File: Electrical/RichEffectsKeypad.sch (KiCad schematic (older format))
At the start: 1 part

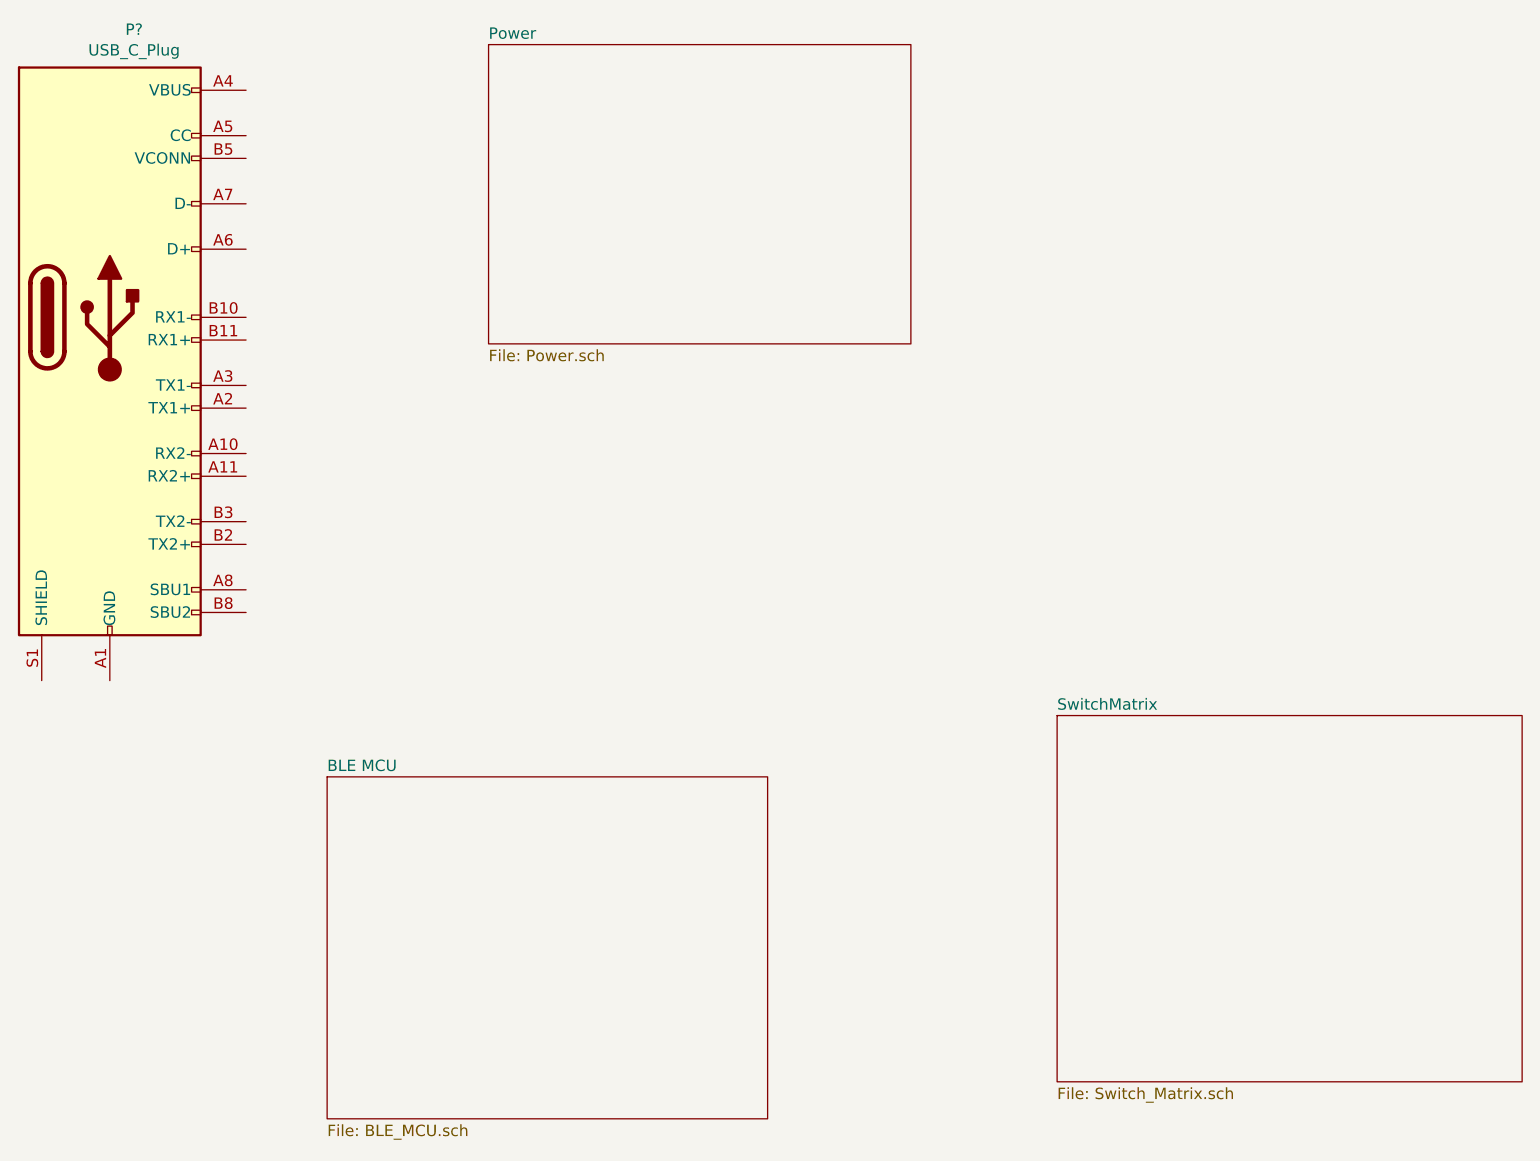
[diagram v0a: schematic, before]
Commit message: USB C and RGB IC Schematics
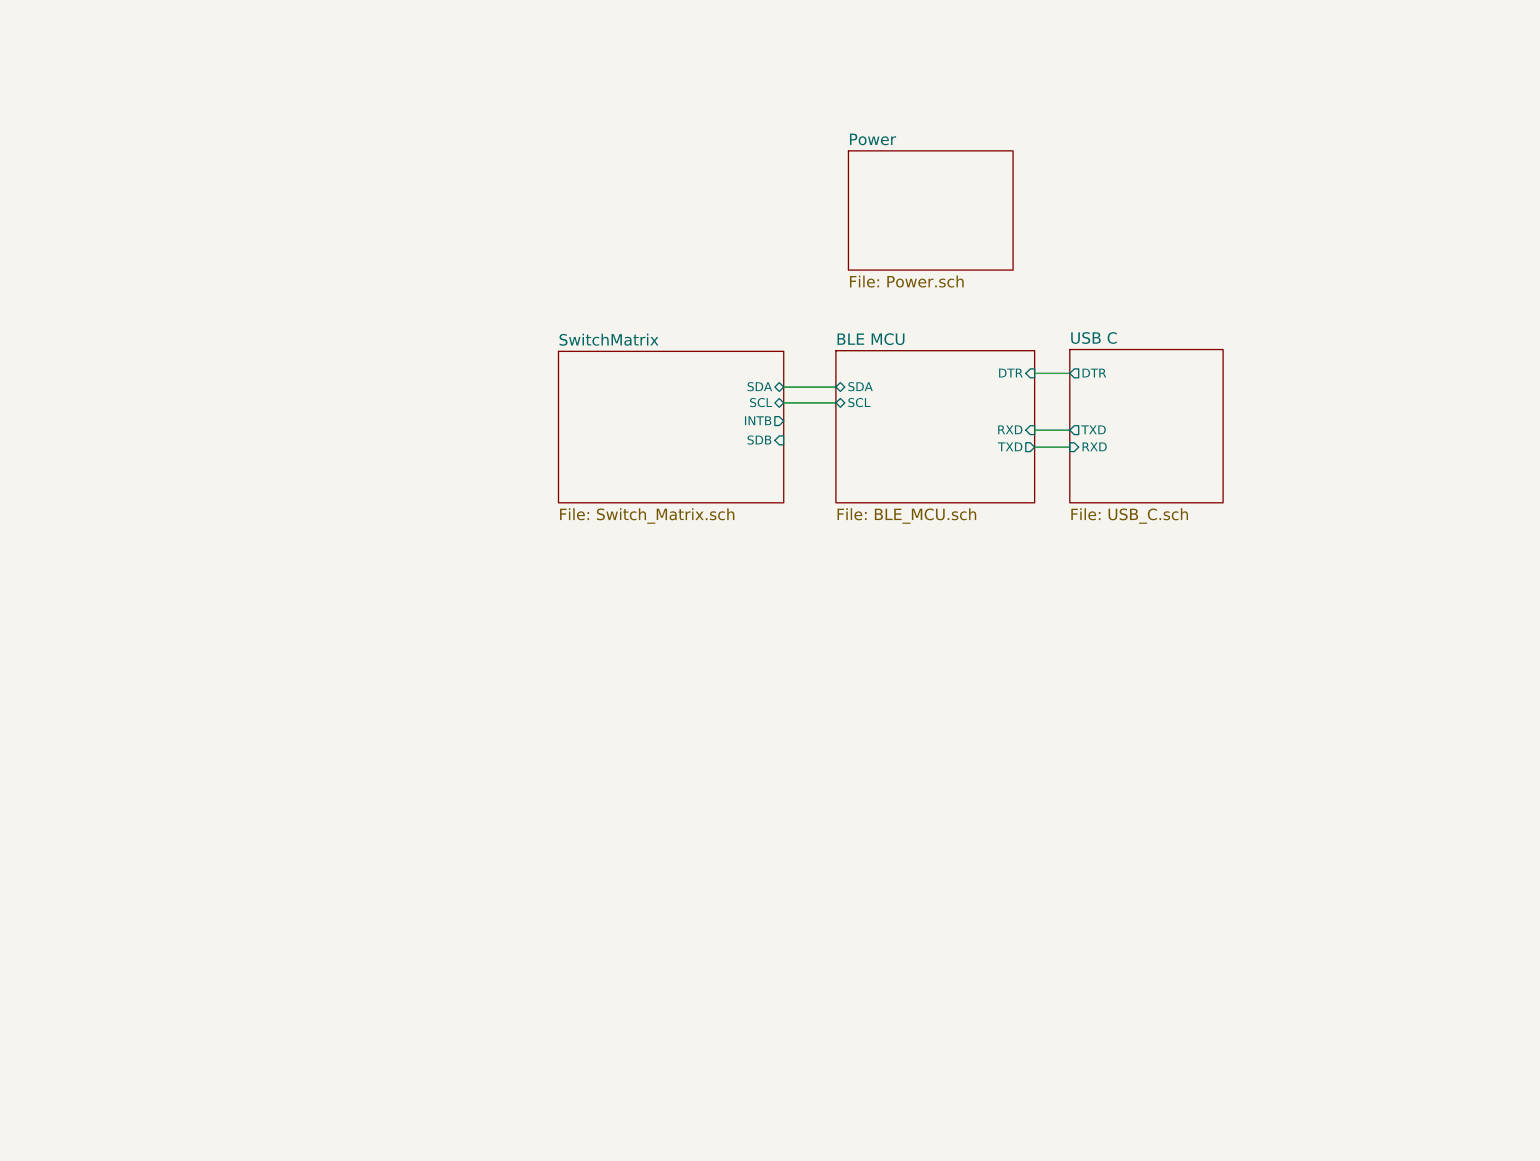
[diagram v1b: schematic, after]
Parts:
- removed P?: USB_C_Plug, symbol Connector:USB_C_Plug
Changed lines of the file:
@@
 $Descr A 11000 8500
 encoding utf-8
-Sheet 1 4
+Sheet 1 5
 Title "Bluetooth5.0 Numpad"
 Date ""
@@
 Comment4 ""
 $EndDescr
-$Comp
-L Connector:USB_C_Plug P?
-U 1 1 60A0497C
-P 1552 2353
-F 0 "P?" H 1659 3620 50  0000 C CNN
-F 1 "USB_C_Plug" H 1659 3529 50  0000 C CNN
-F 2 "" H 1702 2353 50  0001 C CNN
-F 3 "https://www.usb.org/sites/default/files/documents/usb_type-c.zip" H 1702 2353 50  0001 C CNN
-	1    1552 2353
-	1    0    0    -1
-$EndComp
 $Sheet
-S 2509 4377 1940 1506
+S 4750 2500 875  670
 U 60A0B237
 F0 "BLE MCU" 50
 F1 "BLE_MCU.sch" 50
+F2 "DTR" I R 5625 2600 39
+F3 "TXD" O R 5625 2925 39
+F4 "RXD" I R 5625 2850 39
+F5 "SDA" B L 4750 2660 39
+F6 "SCL" B L 4750 2730 39
 $EndSheet
 $Sheet
-S 5724 4107 2048 1613
+S 3528 2503 992  667
 U 60A0DCED
 F0 "SwitchMatrix" 50
 F1 "Switch_Matrix.sch" 50
+F2 "SDA" B R 4520 2660 39
+F3 "SCL" B R 4520 2730 39
+F4 "SDB" I R 4520 2895 39
+F5 "INTB" O R 4520 2810 39
 $EndSheet
 $Sheet
-S 3220 1152 1860 1318
+S 4805 1620 725  525
 U 60A0DD63
 F0 "Power" 50
 F1 "Power.sch" 50
 $EndSheet
+$Sheet
+S 5780 2495 675  675
+U 60A3D900
+F0 "USB C" 50
+F1 "USB_C.sch" 50
+F2 "DTR" O L 5780 2600 39
+F3 "TXD" O L 5780 2850 39
+F4 "RXD" I L 5780 2925 39
+$EndSheet
+Wire Wire Line
+	5625 2850 5780 2850
+Wire Wire Line
+	5780 2925 5625 2925
+Wire Wire Line
+	5625 2600 5780 2600
+Wire Wire Line
+	4750 2660 4520 2660
+Wire Wire Line
+	4750 2730 4520 2730
 $EndSCHEMATC
